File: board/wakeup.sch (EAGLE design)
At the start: 24 parts, among them IC2 ATMEGA48/88/168-AU, K1 PIN20X2, U1 EEPROM24

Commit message: Much better
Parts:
- removed C2: 47nF, rcl:C-EUC0805
- removed CREE_LED1: CREE_XL_MCE, CreeXL-MC-E:CREE_XL_MCE
- removed J1: (no value), con-jack:JACK-PLUG1
- removed UR1, UR2, UR3, UR4, UR5, UR6, UR7, UR8: AMC7135, 1:AMC7135
- added C4: 100nF, rcl:C-EUC0603
- added C5, C6, C7: 10µF, rcl:C-EUC0805
- added CREE_LED2: CREE_XL_MCE, CreeXL-MC-E:CREE_XL_MCE
- added Q5, Q6, Q7, Q8: BC846BSMD, transistor-npn:BC846BSMD
- added R12, R13, R14, R15: 1k, resistor:R-EU_R0603
- added R18, R19, R4, R5: 1k, resistor:R-EU_M0805
- added SL4, SL5, SL6: (no value), con-amp-quick:M04
- added UR10, UR11, UR12, UR13, UR14, UR15, UR16, UR9: AMC7135, 1:AMC7135
- C3: value 47nF -> 100nF; device rcl:C-EUC0805 -> rcl:C-EUC0603
- SL2: device con-amp-quick:M02S -> con-amp-quick:M04
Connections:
- new net ADC0: IC2.PC0(ADC0/PCINT8), SL5.2
- new net GLUMP1: Q5.C, R15.1, UR10.VDD, UR9.VDD
- new net N$4: C4.1, IC2.AREF
- new net N$5: Q8.B, R19.1
- new net N$6: Q7.B, R18.1
- new net N$7: Q5.B, R5.1
- new net N$8: Q6.B, R4.1
- new net SCHMARN1: Q6.C, R14.1, UR11.VDD, UR12.VDD
- new net TEST1: Q7.C, R12.1, UR13.VDD, UR14.VDD
- new net WHITE_LED1: R19.2
- new net ZEUCH1: Q8.C, R13.1, UR15.VDD, UR16.VDD
- net +3V3: now also IC2.AVCC, SL5.3; no longer C2.1, SL2-1.S
- net +5V: now also C5.1, C6.1, C7.1, CREE_LED2G$1.A, CREE_LED2G$2.A, CREE_LED2G$3.A, CREE_LED2G$4.A, CREE_LED2TH.TH, R12.2, R13.2, R14.2, R15.2, SL4.3, SL4.4, SL5.4; no longer J1.3
- net BLUE_LED: now also R18.2; no longer UR5.VDD, UR6.VDD
- net BLUE_LED_OUT: now also CREE_LED2G$2.C, UR13.OUT, UR14.OUT; no longer CREE_LED1G$3.A, UR5.OUT, UR6.OUT
- net GND: now also C4.2, C5.2, C6.2, C7.2, Q5.E, Q6.E, Q7.E, Q8.E, SL4.1, SL4.2, SL5.1, UR10.GND, UR11.GND, UR12.GND, UR13.GND, UR14.GND, UR15.GND, UR16.GND, UR9.GND; no longer C2.2, CREE_LED1G$1.C, CREE_LED1G$2.C, CREE_LED1G$3.C, CREE_LED1G$4.C, CREE_LED1TH.TH, J1.1, J1.2, SL2-2.S, UR1.GND, UR2.GND, UR3.GND, UR4.GND, UR5.GND, UR6.GND, UR7.GND, UR8.GND
- net GREEN_LED: now also R4.2; no longer UR3.VDD, UR4.VDD
- net GREEN_LED_OUT: now also CREE_LED2G$3.C, UR11.OUT, UR12.OUT; no longer CREE_LED1G$2.A, UR3.OUT, UR4.OUT
- net I2C_SCL1: now also IC2.PC5(ADC5/SCL/PCINT13); no longer IC2.PC1(ADC1/PCINT9)
- net I2C_SDA1: now also IC2.PC4(ADC4/SDA/PCINT12); no longer IC2.PC0(ADC0/PCINT8)
- net RED_LED: now also R5.2; no longer UR1.VDD, UR2.VDD
- net RED_LED_OUT: now also CREE_LED2G$4.C, UR10.OUT, UR9.OUT; no longer CREE_LED1G$1.A, UR1.OUT, UR2.OUT
- net WHITE_LED: no longer UR7.VDD, UR8.VDD
- net WHITE_LED_OUT: now also CREE_LED2G$1.C, UR15.OUT, UR16.OUT; no longer CREE_LED1G$4.A, UR7.OUT, UR8.OUT
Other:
- note added: "700mA"
- note added: "EEPROM für Raspy HAT"

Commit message: Fixed some errors
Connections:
- removed net WHITE_LED1: R19.2
- net WHITE_LED: now also R19.2
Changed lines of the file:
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@@
 <grid distance="0.1" unitdist="inch" unit="inch" style="lines" multiple="1" display="no" altdistance="0.01" altunitdist="inch" altunit="inch"/>
 <layers>
-<layer number="1" name="Top" color="4" fill="1" visible="yes" active="no"/>
-<layer number="2" name="Route2" color="1" fill="3" visible="yes" active="no"/>
-<layer number="3" name="Route3" color="4" fill="3" visible="yes" active="no"/>
-<layer number="4" name="Route4" color="1" fill="4" visible="yes" active="no"/>
-<layer number="5" name="Route5" color="4" fill="4" visible="yes" active="no"/>
-<layer number="6" name="Route6" color="1" fill="8" visible="yes" active="no"/>
-<layer number="7" name="Route7" color="4" fill="8" visible="yes" active="no"/>
-<layer number="8" name="Route8" color="1" fill="2" visible="yes" active="no"/>
-<layer number="9" name="Route9" color="4" fill="2" visible="yes" active="no"/>
-<layer number="10" name="Route10" color="1" fill="7" visible="yes" active="no"/>
-<layer number="11" name="Route11" color="4" fill="7" visible="yes" active="no"/>
-<layer number="12" name="Route12" color="1" fill="5" visible="yes" active="no"/>
-<layer number="13" name="Route13" color="4" fill="5" visible="yes" active="no"/>
-<layer number="14" name="Route14" color="1" fill="6" visible="yes" active="no"/>
-<layer number="15" name="Route15" color="4" fill="6" visible="yes" active="no"/>
-<layer number="16" name="Bottom" color="1" fill="1" visible="yes" active="no"/>
-<layer number="17" name="Pads" color="2" fill="1" visible="yes" active="no"/>
-<layer number="18" name="Vias" color="2" fill="1" visible="yes" active="no"/>
-<layer number="19" name="Unrouted" color="6" fill="1" visible="yes" active="no"/>
-<layer number="20" name="Dimension" color="15" fill="1" visible="yes" active="no"/>
-<layer number="21" name="tPlace" color="7" fill="1" visible="yes" active="no"/>
-<layer number="22" name="bPlace" color="7" fill="1" visible="yes" active="no"/>
-<layer number="23" name="tOrigins" color="15" fill="1" visible="yes" active="no"/>
-<layer number="24" name="bOrigins" color="15" fill="1" visible="yes" active="no"/>
-<layer number="25" name="tNames" color="7" fill="1" visible="yes" active="no"/>
-<layer number="26" name="bNames" color="7" fill="1" visible="yes" active="no"/>
-<layer number="27" name="tValues" color="7" fill="1" visible="yes" active="no"/>
-<layer number="28" name="bValues" color="7" fill="1" visible="yes" active="no"/>
+<layer number="1" name="Top" color="4" fill="1" visible="no" active="no"/>
+<layer number="2" name="Route2" color="1" fill="3" visible="no" active="no"/>
+<layer number="3" name="Route3" color="4" fill="3" visible="no" active="no"/>
+<layer number="4" name="Route4" color="1" fill="4" visible="no" active="no"/>
+<layer number="5" name="Route5" color="4" fill="4" visible="no" active="no"/>
+<layer number="6" name="Route6" color="1" fill="8" visible="no" active="no"/>
+<layer number="7" name="Route7" color="4" fill="8" visible="no" active="no"/>
+<layer number="8" name="Route8" color="1" fill="2" visible="no" active="no"/>
+<layer number="9" name="Route9" color="4" fill="2" visible="no" active="no"/>
+<layer number="10" name="Route10" color="1" fill="7" visible="no" active="no"/>
+<layer number="11" name="Route11" color="4" fill="7" visible="no" active="no"/>
+<layer number="12" name="Route12" color="1" fill="5" visible="no" active="no"/>
+<layer number="13" name="Route13" color="4" fill="5" visible="no" active="no"/>
+<layer number="14" name="Route14" color="1" fill="6" visible="no" active="no"/>
+<layer number="15" name="Route15" color="4" fill="6" visible="no" active="no"/>
+<layer number="16" name="Bottom" color="1" fill="1" visible="no" active="no"/>
+<layer number="17" name="Pads" color="2" fill="1" visible="no" active="no"/>
+<layer number="18" name="Vias" color="2" fill="1" visible="no" active="no"/>
+<layer number="19" name="Unrouted" color="6" fill="1" visible="no" active="no"/>
+<layer number="20" name="Dimension" color="15" fill="1" visible="no" active="no"/>
+<layer number="21" name="tPlace" color="7" fill="1" visible="no" active="no"/>
+<layer number="22" name="bPlace" color="7" fill="1" visible="no" active="no"/>
+<layer number="23" name="tOrigins" color="15" fill="1" visible="no" active="no"/>
+<layer number="24" name="bOrigins" color="15" fill="1" visible="no" active="no"/>
+<layer number="25" name="tNames" color="7" fill="1" visible="no" active="no"/>
+<layer number="26" name="bNames" color="7" fill="1" visible="no" active="no"/>
+<layer number="27" name="tValues" color="7" fill="1" visible="no" active="no"/>
+<layer number="28" name="bValues" color="7" fill="1" visible="no" active="no"/>
 <layer number="29" name="tStop" color="7" fill="3" visible="no" active="no"/>
 <layer number="30" name="bStop" color="7" fill="6" visible="no" active="no"/>
@@
 <layer number="35" name="tGlue" color="7" fill="4" visible="no" active="no"/>
 <layer number="36" name="bGlue" color="7" fill="5" visible="no" active="no"/>
-<layer number="37" name="tTest" color="7" fill="1" visible="yes" active="no"/>
-<layer number="38" name="bTest" color="7" fill="1" visible="yes" active="no"/>
+<layer number="37" name="tTest" color="7" fill="1" visible="no" active="no"/>
+<layer number="38" name="bTest" color="7" fill="1" visible="no" active="no"/>
 <layer number="39" name="tKeepout" color="4" fill="11" visible="no" active="no"/>
 <layer number="40" name="bKeepout" color="1" fill="11" visible="no" active="no"/>
@@
 <layer number="44" name="Drills" color="7" fill="1" visible="no" active="no"/>
 <layer number="45" name="Holes" color="7" fill="1" visible="no" active="no"/>
-<layer number="46" name="Milling" color="3" fill="1" visible="yes" active="no"/>
-<layer number="47" name="Measures" color="7" fill="1" visible="yes" active="no"/>
-<layer number="48" name="Document" color="7" fill="1" visible="yes" active="no"/>
-<layer number="49" name="Reference" color="7" fill="1" visible="yes" active="no"/>
-<layer number="50" name="dxf" color="7" fill="1" visible="yes" active="no"/>
-<layer number="51" name="tDocu" color="7" fill="1" visible="yes" active="no"/>
-<layer number="52" name="bDocu" color="7" fill="1" visible="yes" active="no"/>
-<layer number="53" name="tGND_GNDA" color="7" fill="1" visible="yes" active="no"/>
-<layer number="54" name="bGND_GNDA" color="7" fill="1" visible="yes" active="no"/>
-<layer number="56" name="wert" color="7" fill="1" visible="yes" active="no"/>
+<layer number="46" name="Milling" color="3" fill="1" visible="no" active="no"/>
+<layer number="47" name="Measures" color="7" fill="1" visible="no" active="no"/>
+<layer number="48" name="Document" color="7" fill="1" visible="no" active="no"/>
+<layer number="49" name="Reference" color="7" fill="1" visible="no" active="no"/>
+<layer number="50" name="dxf" color="7" fill="1" visible="no" active="no"/>
+<layer number="51" name="tDocu" color="7" fill="1" visible="no" active="no"/>
+<layer number="52" name="bDocu" color="7" fill="1" visible="no" active="no"/>
+<layer number="53" name="tGND_GNDA" color="7" fill="1" visible="no" active="no"/>
+<layer number="54" name="bGND_GNDA" color="7" fill="1" visible="no" active="no"/>
+<layer number="56" name="wert" color="7" fill="1" visible="no" active="no"/>
 <layer number="90" name="Modules" color="5" fill="1" visible="yes" active="yes"/>
 <layer number="91" name="Nets" color="2" fill="1" visible="yes" active="yes"/>
@@
 </segment>
 </net>
-<net name="WHITE_LED1" class="0">
+<net name="WHITE_LED" class="0">
 <segment>
 <wire x1="27.94" y1="38.1" x2="43.18" y2="38.1" width="0.1524" layer="91"/>

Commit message: Finalized Updates
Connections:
- net GLUMP1 renamed RED_POWER
- net SCHMARN1 renamed GREEN_POWER
- net TEST1 renamed BLUE_POWER
- net ZEUCH1 renamed WHITE_POWER
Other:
- moved on the sheet: C3, C4, IC2, SL1, SL3, SV1

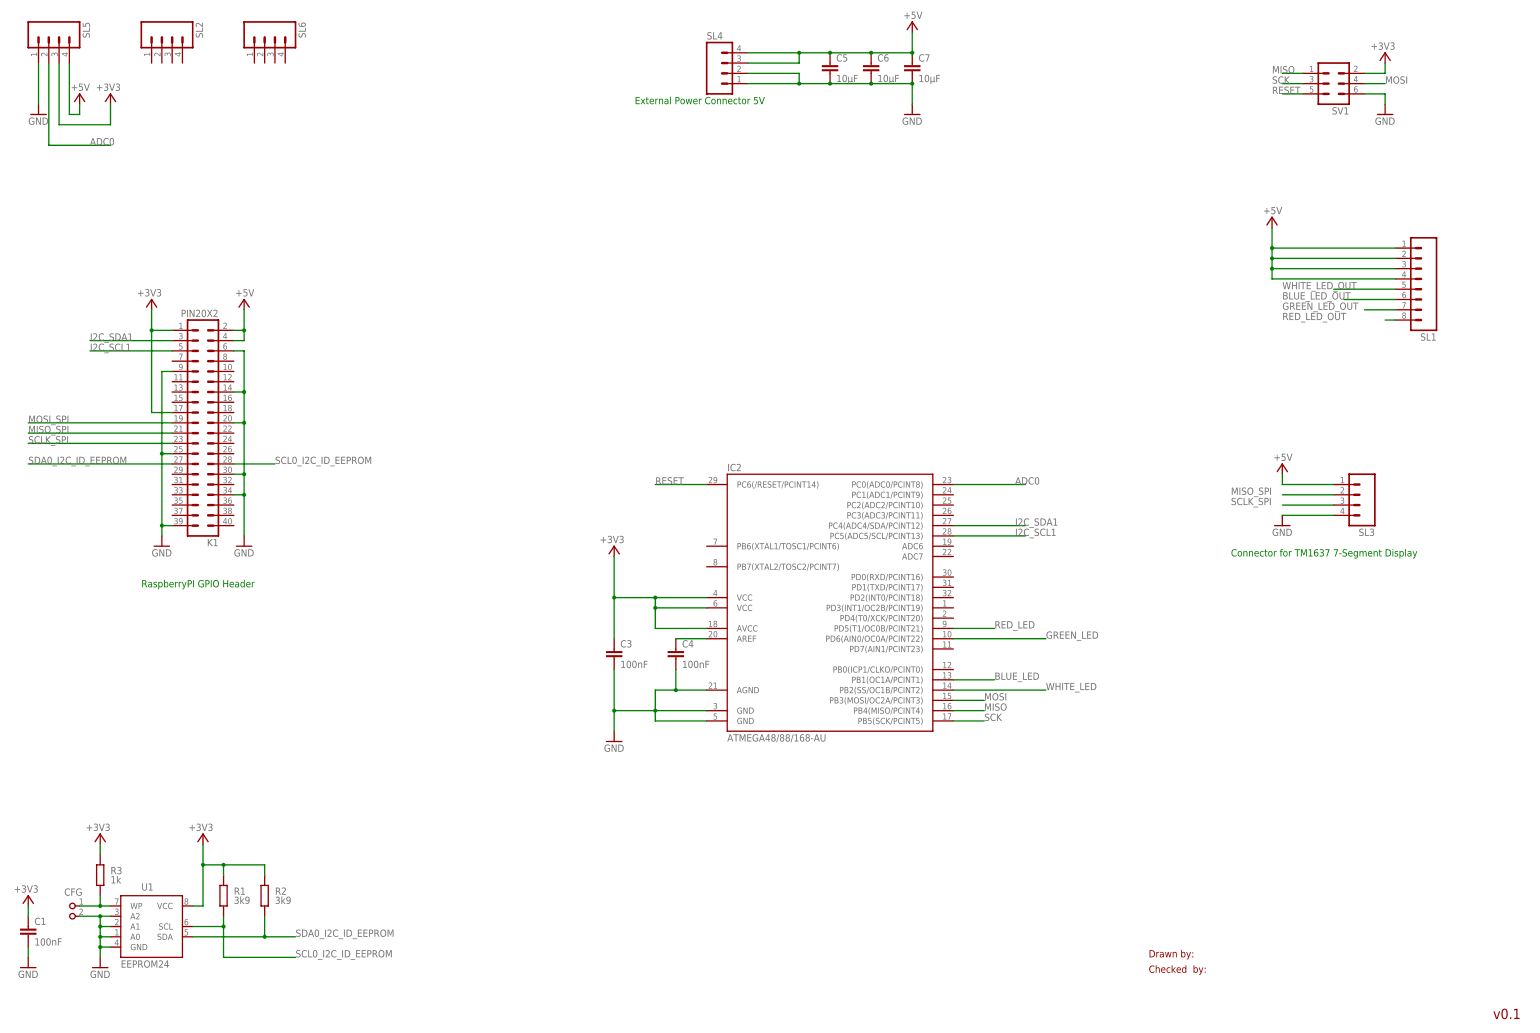
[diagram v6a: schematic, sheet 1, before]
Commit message: Finalized board. Readded CON_JACK
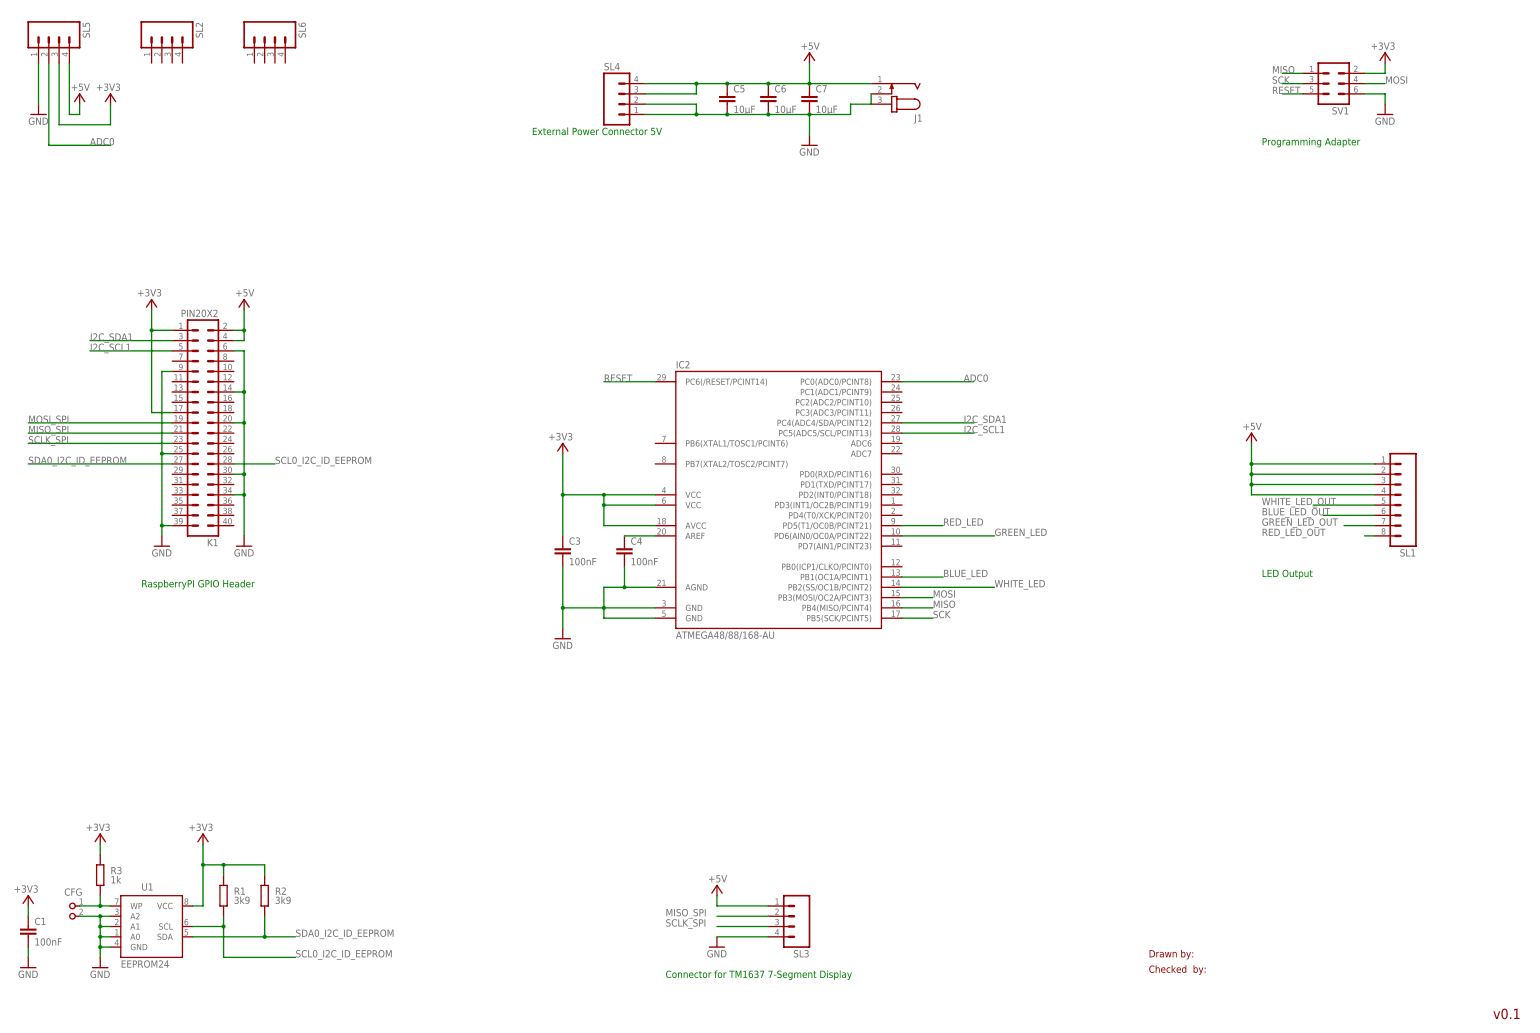
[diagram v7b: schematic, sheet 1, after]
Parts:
- added J1: (no value), con-jack:JACK-PLUG1
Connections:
- net +5V: now also J1.1
- net GND: now also J1.2, J1.3
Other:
- note added: "LED Output"
- note added: "Programming Adapter"
- moved on the sheet: C3, C4, C5, C6, C7, IC2, SL1, SL3, SL4
